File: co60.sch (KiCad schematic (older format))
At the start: 18 parts, among them SW1 SW_Push, U1 ATMEGA32U4-AU, X1 ASX3F

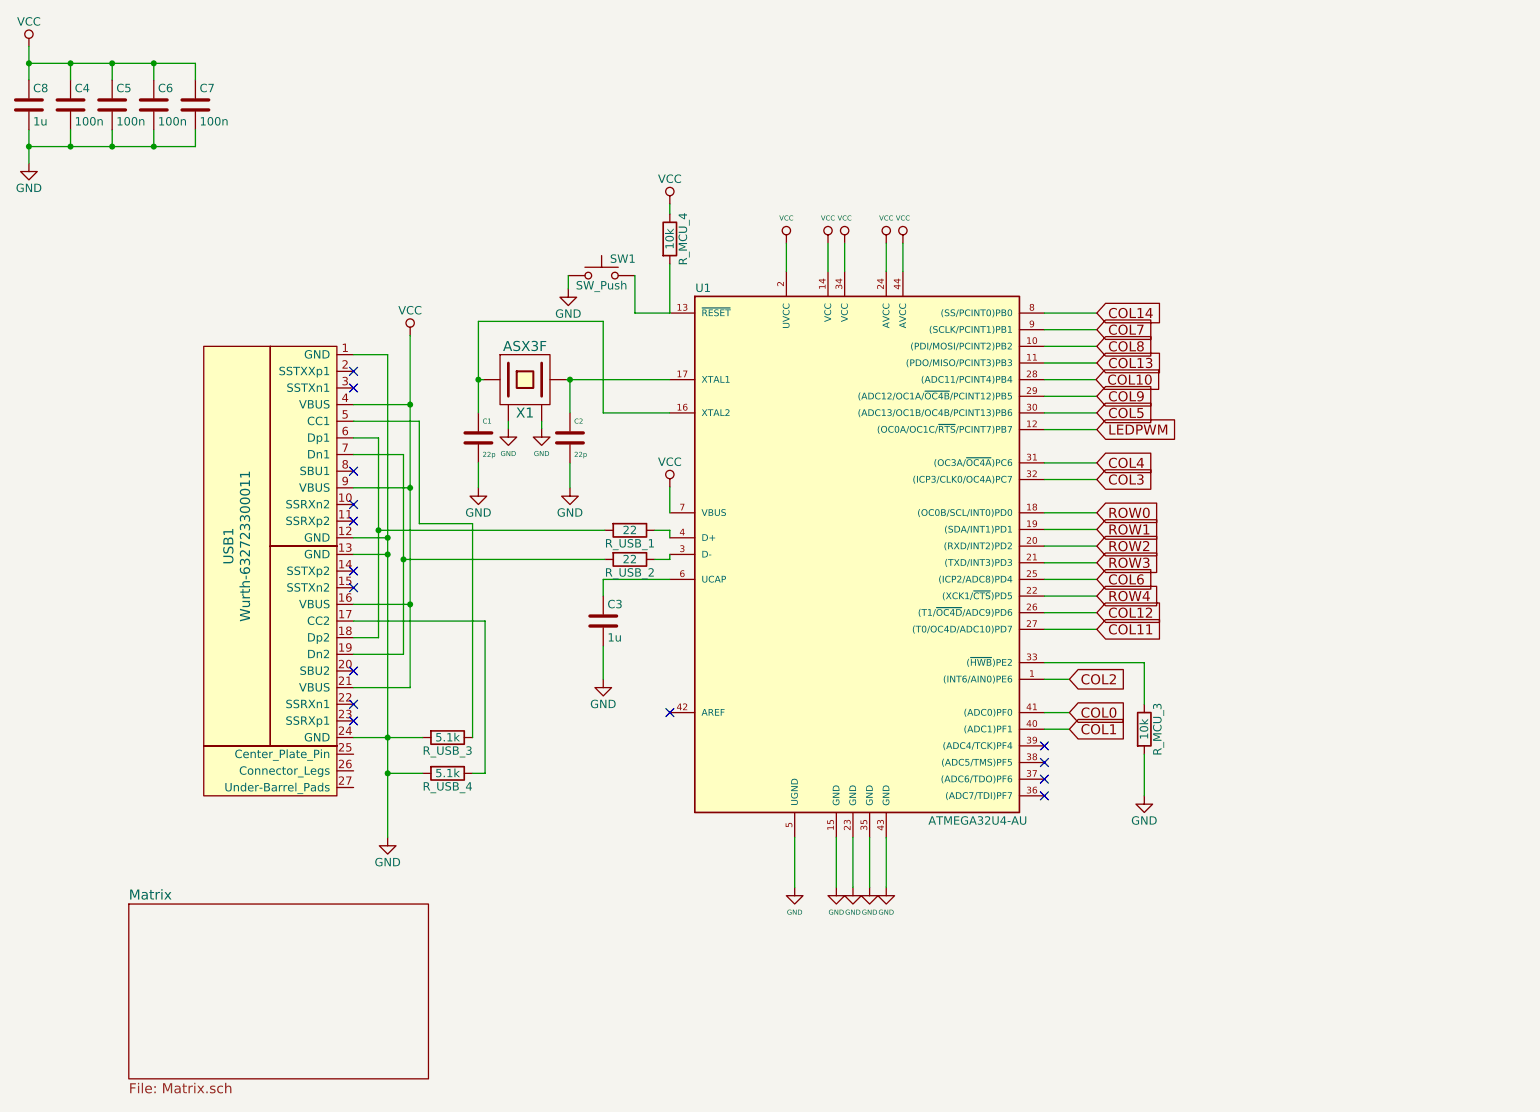
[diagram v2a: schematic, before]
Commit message: Fix schematic errors, add datasheet links, and transistor for LEDs
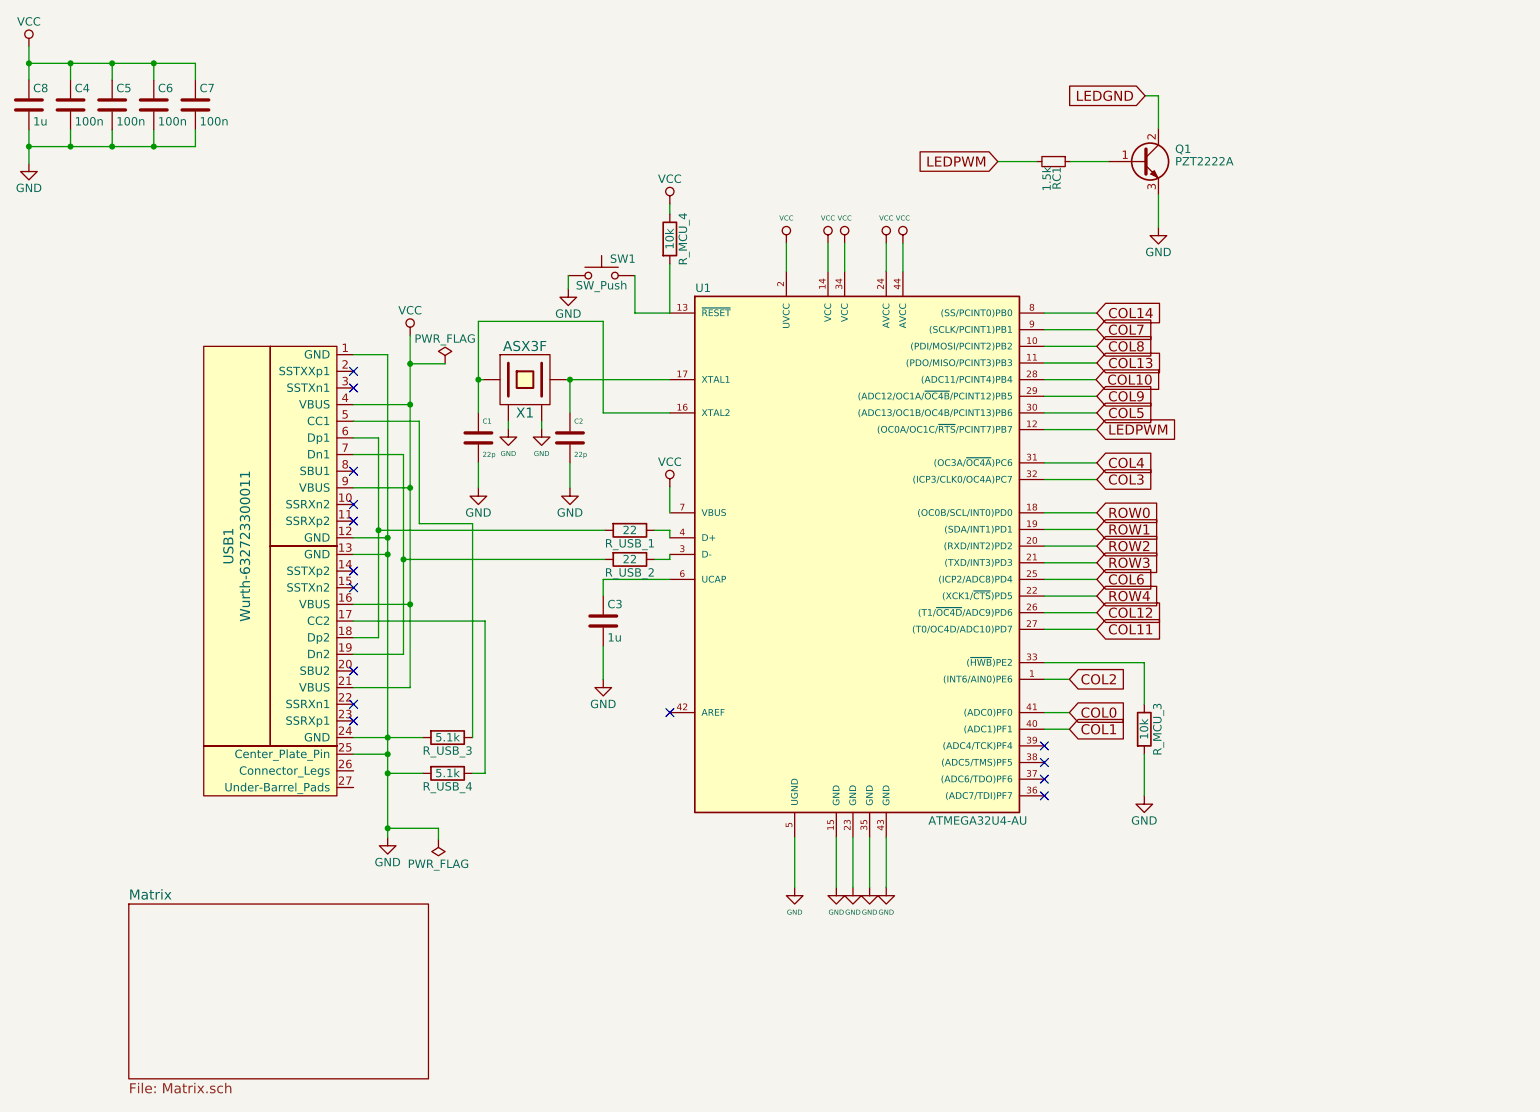
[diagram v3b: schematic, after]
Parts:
- added Q1: PZT2222A, TO_SOT_Packages_SMD:SOT-223, symbol PZT2222A
- added RC1: 1.5k, symbol R_Small
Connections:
- net GND: now also USB1.25 (Center_Plate_Pin), Q1.3 (E)
- net LEDPWM: now also RC1.2
- new net: Q1.1 (B), RC1.1
- new net LEDGND: Q1.2 (C)
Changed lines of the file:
@@
 F 1 "ATMEGA32U4-AU" H 6600 2350 50  0000 C CNN
 F 2 "TQFP44" H 5900 3850 50  0001 C CIN
-F 3 "" H 7000 4950 50  0001 C CNN
+F 3 "http://ww1.microchip.com/downloads/en/DeviceDoc/Atmel-7766-8-bit-AVR-ATmega16U4-32U4_Summary.pdf" H 7000 4950 50  0001 C CNN
 	1    5900 3850
 	1    0    0    -1
@@
 F 1 "Wurth-632723300011" V 2200 3700 60  0000 C CNN
 F 2 "" H 2750 3700 60  0001 C CNN
-F 3 "" H 2750 3700 60  0001 C CNN
+F 3 "http://katalog.we-online.de/em/datasheet/632723x00011.pdf" H 2750 3700 60  0001 C CNN
 	1    2750 3700
 	1    0    0    -1
@@
 F 1 "ASX3F" H 3880 2900 60  0000 C CNN
 F 2 "" H 3880 2700 60  0001 C CNN
-F 3 "" H 3880 2700 60  0001 C CNN
+F 3 "http://www.ansenquartz.com/Upload/Products/Pro-20151234634734.pdf" H 3880 2700 60  0001 C CNN
 	1    3880 2700
 	1    0    0    -1
@@
 	4540 2300 4750 2300
 $Comp
-L GND #PWR?
+L GND #PWR023
 U 1 1 5AC1F377
 P 4140 2155
-F 0 "#PWR?" H 4140 1905 50  0001 C CNN
+F 0 "#PWR023" H 4140 1905 50  0001 C CNN
 F 1 "GND" H 4140 2005 50  0000 C CNN
 F 2 "" H 4140 2155 50  0001 C CNN
@@
 Wire Wire Line
 	4140 2075 4140 2155
+$Comp
+L PZT2222A Q1
+U 1 1 5AC26B07
+P 7585 1390
+F 0 "Q1" H 7785 1465 50  0000 L CNN
+F 1 "PZT2222A" H 7785 1390 50  0000 L CNN
+F 2 "TO_SOT_Packages_SMD:SOT-223" H 7785 1315 50  0001 L CIN
+F 3 "http://www.onsemi.com/pub/Collateral/PZT2222AT1-D.PDF" H 7585 1390 50  0001 L CNN
+	1    7585 1390
+	1    0    0    -1
+$EndComp
+Text GLabel 6720 1390 0    60   Input ~ 0
+LEDPWM
+Text GLabel 7605 995  0    60   Input ~ 0
+LEDGND
+$Comp
+L GND #PWR024
+U 1 1 5AC27CFC
+P 7685 1785
+F 0 "#PWR024" H 7685 1535 50  0001 C CNN
+F 1 "GND" H 7685 1635 50  0000 C CNN
+F 2 "" H 7685 1785 50  0001 C CNN
+F 3 "" H 7685 1785 50  0001 C CNN
+	1    7685 1785
+	1    0    0    -1
+$EndComp
+Wire Wire Line
+	7685 1590 7685 1785
+Wire Wire Line
+	7605 995  7685 995
+Wire Wire Line
+	7685 995  7685 1190
+$Comp
+L R_Small RC1
+U 1 1 5AC284AA
+P 7055 1390
+F 0 "RC1" H 7085 1410 50  0000 L CNN
+F 1 "1.5k" H 7085 1350 50  0000 L CNN
+F 2 "" H 7055 1390 50  0001 C CNN
+F 3 "" H 7055 1390 50  0001 C CNN
+	1    7055 1390
+	0    1    1    0
+$EndComp
+Wire Wire Line
+	6720 1390 6955 1390
+Wire Wire Line
+	7155 1390 7385 1390
+$Comp
+L PWR_FLAG #FLG025
+U 1 1 5AC2942E
+P 3400 2605
+F 0 "#FLG025" H 3400 2680 50  0001 C CNN
+F 1 "PWR_FLAG" H 3400 2755 50  0000 C CNN
+F 2 "" H 3400 2605 50  0001 C CNN
+F 3 "" H 3400 2605 50  0001 C CNN
+	1    3400 2605
+	1    0    0    -1
+$EndComp
+Wire Wire Line
+	3400 2605 3190 2605
+Connection ~ 3190 2605
+$Comp
+L PWR_FLAG #FLG026
+U 1 1 5AC2A5F1
+P 3360 5460
+F 0 "#FLG026" H 3360 5535 50  0001 C CNN
+F 1 "PWR_FLAG" H 3360 5610 50  0000 C CNN
+F 2 "" H 3360 5460 50  0001 C CNN
+F 3 "" H 3360 5460 50  0001 C CNN
+	1    3360 5460
+	-1   0    0    1
+$EndComp
+Wire Wire Line
+	3360 5460 3360 5395
+Wire Wire Line
+	3360 5395 3055 5395
+Connection ~ 3055 5395
+Wire Wire Line
+	2850 4950 3055 4950
+Connection ~ 3055 4950
 $EndSCHEMATC

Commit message: Update: Switch atmega32u4 to gh60 version of the component
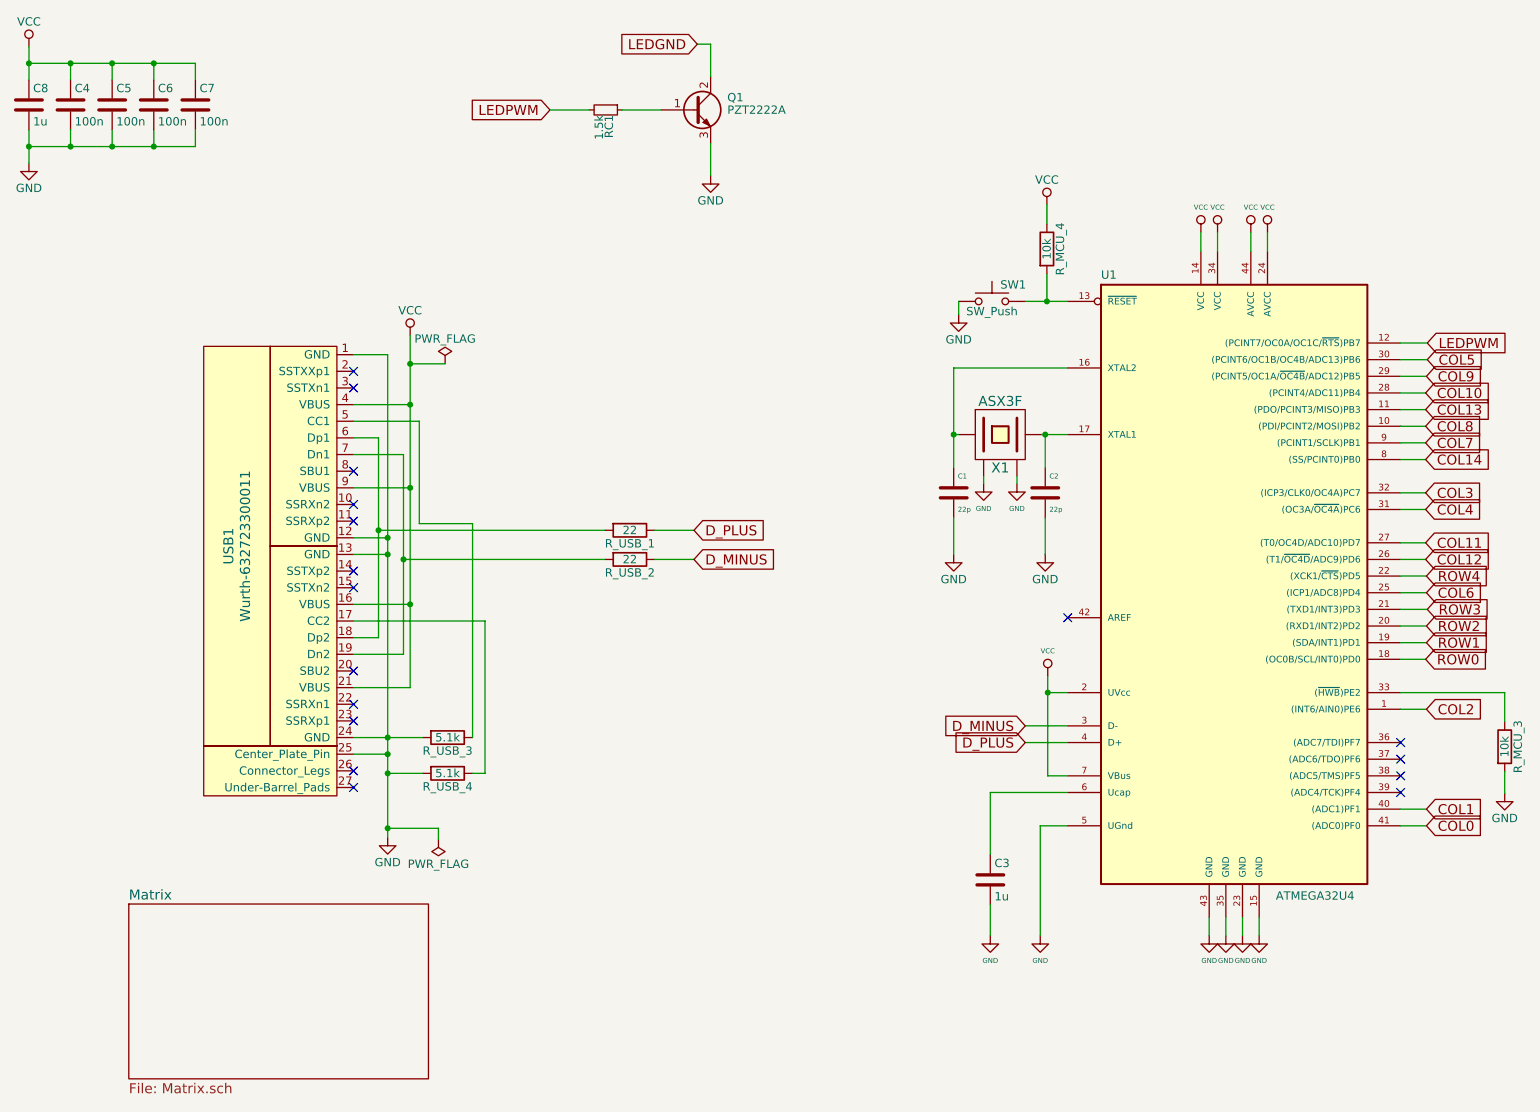
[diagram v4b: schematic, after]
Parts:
- removed U1: ATMEGA32U4-AU, TQFP44, symbol ATMEGA32U4-AU
- added U1: ATMEGA32U4, TQFP44, symbol ATMEGA32U4
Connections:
- net COL0: now also U1.41 ((ADC0)PF0)
- net COL1: now also U1.40 ((ADC1)PF1)
- net COL10: now also U1.28 ((PCINT4/ADC11)PB4)
- net COL11: now also U1.27 ((T0/OC4D/ADC10)PD7)
- net COL12: now also U1.26 ((T1/~OC4D~/ADC9)PD6)
- net COL13: now also U1.11 ((PDO/PCINT3/MISO)PB3)
- net COL14: now also U1.8 ((SS/PCINT0)PB0)
- net COL2: now also U1.1 ((INT6/AIN0)PE6)
- net COL3: now also U1.32 ((ICP3/CLK0/OC4A)PC7)
- net COL4: now also U1.31 ((OC3A/~OC4A~)PC6)
- net COL5: now also U1.30 ((PCINT6/OC1B/OC4B/ADC13)PB6)
- net COL6: now also U1.25 ((ICP1/ADC8)PD4)
- net COL7: now also U1.9 ((PCINT1/SCLK)PB1)
- net COL8: now also U1.10 ((PDI/PCINT2/MOSI)PB2)
- net COL9: now also U1.29 ((PCINT5/OC1A/~OC4B~/ADC12)PB5)
- net GND: now also U1.15 (GND), U1.23 (GND), U1.35 (GND), U1.43 (GND), U1.5 (UGnd)
- net LEDPWM: now also U1.12 ((PCINT7/OC0A/OC1C/~RTS~)PB7)
- net ROW0: now also U1.18 ((OC0B/SCL/INT0)PD0)
- net ROW1: now also U1.19 ((SDA/INT1)PD1)
- net ROW2: now also U1.20 ((RXD1/INT2)PD2)
- net ROW3: now also U1.21 ((TXD1/INT3)PD3)
- net ROW4: now also U1.22 ((XCK1/~CTS~)PD5)
- net VCC: now also U1.14 (VCC), U1.2 (UVcc), U1.24 (AVCC), U1.34 (VCC), U1.44 (AVCC), U1.7 (VBus)
- net at R_MCU_4.2, SW1.2: now also U1.13 (~RESET~)
- net at C1.1, X1.1: now also U1.16 (XTAL2)
- net at C2.1, X1.3 (2): now also U1.17 (XTAL1)
- net D_MINUS: now reaches R_USB_2.1
- net D_MINUS: now also U1.3 (D-)
- net at R_MCU_3.1: now also U1.33 ((~HWB~)PE2)
- net D_PLUS: now reaches R_USB_1.1
- net D_PLUS: now also U1.4 (D+)
- net at C3.1: now also U1.6 (Ucap)
- no-connect marks 15 -> 17
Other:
- moved on the sheet: C1, C2, C3, Q1, RC1, R_MCU_3, R_MCU_4, SW1, X1

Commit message: Update: Work on schematic for bottom row
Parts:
- C1, C2, C3, C4, C5, C6, C7, C8: footprint (none) -> Capacitors_SMD:C_0603
- RC1, R_MCU_3, R_MCU_4, R_USB_1, R_USB_2, R_USB_3, R_USB_4: footprint (none) -> Resistors_SMD:R_0603
- U1: footprint TQFP44 -> tqfp:TQFP44
- USB1: footprint (none) -> Type-C:Wurth-632723300011
- X1: footprint (none) -> ndk:4-SMD
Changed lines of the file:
@@
 F 0 "C2" H 7030 3480 30  0000 L CNN
 F 1 "22p" H 7030 3280 30  0000 L CNN
-F 2 "" H 7043 3230 50  0001 C CNN
+F 2 "Capacitors_SMD:C_0603" H 7043 3230 50  0001 C CNN
 F 3 "" H 7005 3380 50  0001 C CNN
 	1    7005 3380
@@
 F 0 "C1" H 6480 3480 30  0000 L CNN
 F 1 "22p" H 6480 3280 30  0000 L CNN
-F 2 "" H 6493 3230 50  0001 C CNN
+F 2 "Capacitors_SMD:C_0603" H 6493 3230 50  0001 C CNN
 F 3 "" H 6455 3380 50  0001 C CNN
 	1    6455 3380
@@
 F 0 "C3" H 6700 5805 50  0000 L CNN
 F 1 "1u" H 6700 5605 50  0000 L CNN
-F 2 "" H 6713 5555 50  0001 C CNN
+F 2 "Capacitors_SMD:C_0603" H 6713 5555 50  0001 C CNN
 F 3 "" H 6675 5705 50  0001 C CNN
 	1    6675 5705
@@
 F 0 "C4" H 1175 1150 50  0000 L CNN
 F 1 "100n" H 1175 950 50  0000 L CNN
-F 2 "" H 1188 900 50  0001 C CNN
+F 2 "Capacitors_SMD:C_0603" H 1188 900 50  0001 C CNN
 F 3 "" H 1150 1050 50  0001 C CNN
 	1    1150 1050
@@
 F 0 "C5" H 1425 1150 50  0000 L CNN
 F 1 "100n" H 1425 950 50  0000 L CNN
-F 2 "" H 1438 900 50  0001 C CNN
+F 2 "Capacitors_SMD:C_0603" H 1438 900 50  0001 C CNN
 F 3 "" H 1400 1050 50  0001 C CNN
 	1    1400 1050
@@
 F 0 "C6" H 1675 1150 50  0000 L CNN
 F 1 "100n" H 1675 950 50  0000 L CNN
-F 2 "" H 1688 900 50  0001 C CNN
+F 2 "Capacitors_SMD:C_0603" H 1688 900 50  0001 C CNN
 F 3 "" H 1650 1050 50  0001 C CNN
 	1    1650 1050
@@
 F 0 "C7" H 1925 1150 50  0000 L CNN
 F 1 "100n" H 1925 950 50  0000 L CNN
-F 2 "" H 1938 900 50  0001 C CNN
+F 2 "Capacitors_SMD:C_0603" H 1938 900 50  0001 C CNN
 F 3 "" H 1900 1050 50  0001 C CNN
 	1    1900 1050
@@
 F 0 "C8" H 925 1150 50  0000 L CNN
 F 1 "1u" H 925 950 50  0000 L CNN
-F 2 "" H 938 900 50  0001 C CNN
+F 2 "Capacitors_SMD:C_0603" H 938 900 50  0001 C CNN
 F 3 "" H 900 1050 50  0001 C CNN
 	1    900  1050
@@
 F 0 "USB1" V 2100 3700 60  0000 C CNN
 F 1 "Wurth-632723300011" V 2200 3700 60  0000 C CNN
-F 2 "" H 2750 3700 60  0001 C CNN
+F 2 "Type-C:Wurth-632723300011" H 2750 3700 60  0001 C CNN
 F 3 "http://katalog.we-online.de/em/datasheet/632723x00011.pdf" H 2750 3700 60  0001 C CNN
 	1    2750 3700
@@
 F 0 "R_MCU_3" V 9845 4905 50  0000 C CNN
 F 1 "10k" V 9765 4905 50  0000 C CNN
-F 2 "" V 9695 4905 50  0001 C CNN
+F 2 "Resistors_SMD:R_0603" V 9695 4905 50  0001 C CNN
 F 3 "" H 9765 4905 50  0001 C CNN
 	1    9765 4905
@@
 F 0 "X1" H 6735 2830 60  0000 C CNN
 F 1 "ASX3F" H 6735 3230 60  0000 C CNN
-F 2 "" H 6735 3030 60  0001 C CNN
+F 2 "ndk:4-SMD" H 6735 3030 60  0001 C CNN
 F 3 "http://www.ansenquartz.com/Upload/Products/Pro-20151234634734.pdf" H 6735 3030 60  0001 C CNN
 	1    6735 3030
@@
 F 0 "R_USB_1" V 4590 3605 50  0000 C CNN
 F 1 "22" V 4510 3605 50  0000 C CNN
-F 2 "" V 4440 3605 50  0001 C CNN
+F 2 "Resistors_SMD:R_0603" V 4440 3605 50  0001 C CNN
 F 3 "" H 4510 3605 50  0001 C CNN
 	1    4510 3605
@@
 F 0 "R_USB_2" V 4590 3780 50  0000 C CNN
 F 1 "22" V 4510 3780 50  0000 C CNN
-F 2 "" V 4440 3780 50  0001 C CNN
+F 2 "Resistors_SMD:R_0603" V 4440 3780 50  0001 C CNN
 F 3 "" H 4510 3780 50  0001 C CNN
 	1    4510 3780
@@
 F 0 "R_USB_3" V 3495 4850 50  0000 C CNN
 F 1 "5.1k" V 3415 4850 50  0000 C CNN
-F 2 "" V 3345 4850 50  0001 C CNN
+F 2 "Resistors_SMD:R_0603" V 3345 4850 50  0001 C CNN
 F 3 "" H 3415 4850 50  0001 C CNN
 	1    3415 4850
@@
 F 0 "R_USB_4" V 3495 5065 50  0000 C CNN
 F 1 "5.1k" V 3415 5065 50  0000 C CNN
-F 2 "" V 3345 5065 50  0001 C CNN
+F 2 "Resistors_SMD:R_0603" V 3345 5065 50  0001 C CNN
 F 3 "" H 3415 5065 50  0001 C CNN
 	1    3415 5065
@@
 F 0 "R_MCU_4" V 7095 1915 50  0000 C CNN
 F 1 "10k" V 7015 1915 50  0000 C CNN
-F 2 "" V 6945 1915 50  0001 C CNN
+F 2 "Resistors_SMD:R_0603" V 6945 1915 50  0001 C CNN
 F 3 "" H 7015 1915 50  0001 C CNN
 	1    7015 1915
@@
 F 0 "RC1" H 4395 1100 50  0000 L CNN
 F 1 "1.5k" H 4395 1040 50  0000 L CNN
-F 2 "" H 4365 1080 50  0001 C CNN
+F 2 "Resistors_SMD:R_0603" H 4365 1080 50  0001 C CNN
 F 3 "" H 4365 1080 50  0001 C CNN
 	1    4365 1080
@@
 F 0 "U1" H 7340 5760 50  0000 L BNN
 F 1 "ATMEGA32U4" H 8390 2030 50  0000 L BNN
-F 2 "TQFP44" H 8640 1955 50  0001 C CNN
-F 3 "" H 8140 3930 60  0001 C CNN
+F 2 "tqfp:TQFP44" H 8640 1955 50  0001 C CNN
+F 3 "http://ww1.microchip.com/downloads/en/DeviceDoc/Atmel-7766-8-bit-AVR-ATmega16U4-32U4_Summary.pdf" H 8140 3930 60  0001 C CNN
 	1    8140 3930
 	1    0    0    -1
